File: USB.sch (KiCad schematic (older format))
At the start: 23 parts, among them J302 USB_B_Micro, Q301 SS8050-G, Q302 SS8050-G, Q303 SS8050-G, U301 CP2102N-A01-GQFN24

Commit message: libs added
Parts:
- D302: symbol ESP-Audio-rescue:SP0503BAHT-Power_Protection -> ESP32-Eurorack-Audio-rescue:SP0503BAHT-Power_Protection-ESP-Audio-rescue
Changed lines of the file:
@@
 EESchema Schematic File Version 4
+LIBS:ESP32-Eurorack-Audio-cache
 EELAYER 29 0
 EELAYER END
@@
 	3200 3250 3700 3250
 $Comp
-L ESP-Audio-rescue:SP0503BAHT-Power_Protection D302
+L ESP32-Eurorack-Audio-rescue:SP0503BAHT-Power_Protection-ESP-Audio-rescue D302
 U 1 1 5B67424B
 P 3550 4000

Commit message: current
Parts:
- L301: value 600 -> 0
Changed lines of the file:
@@
 Title "ESP32 Eurorack Audio Module"
 Date "2019-03-27"
-Rev "B2-public"
+Rev "C"
 Comp "(c) Robert Manzke 2019"
 Comment1 "https://creativecommons.org/licenses/by-nc-sa/4.0/"
@@
 P 2900 4300
 F 0 "L301" H 3037 4346 50  0000 L CNN
-F 1 "600" H 3037 4255 50  0000 L CNN
+F 1 "0" H 3037 4255 50  0000 L CNN
 F 2 "Capacitor_SMD:C_0805_2012Metric" V 2830 4300 50  0001 C CNN
 F 3 "~" H 2900 4300 50  0001 C CNN

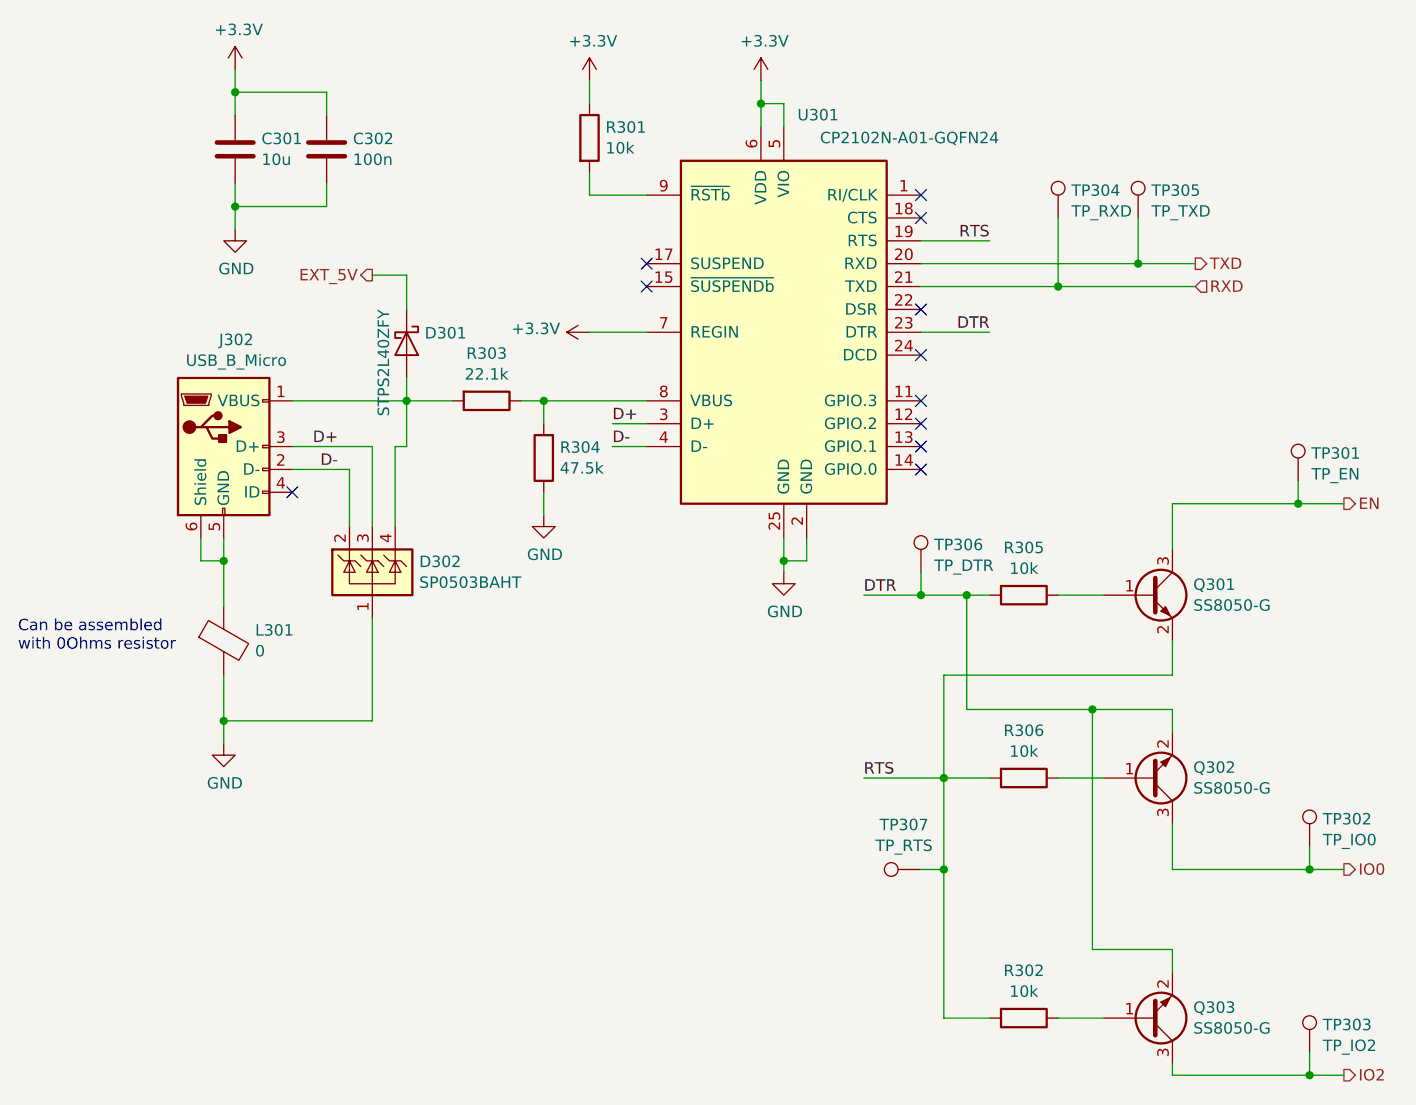
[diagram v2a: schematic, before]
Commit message: cleaned up schematic
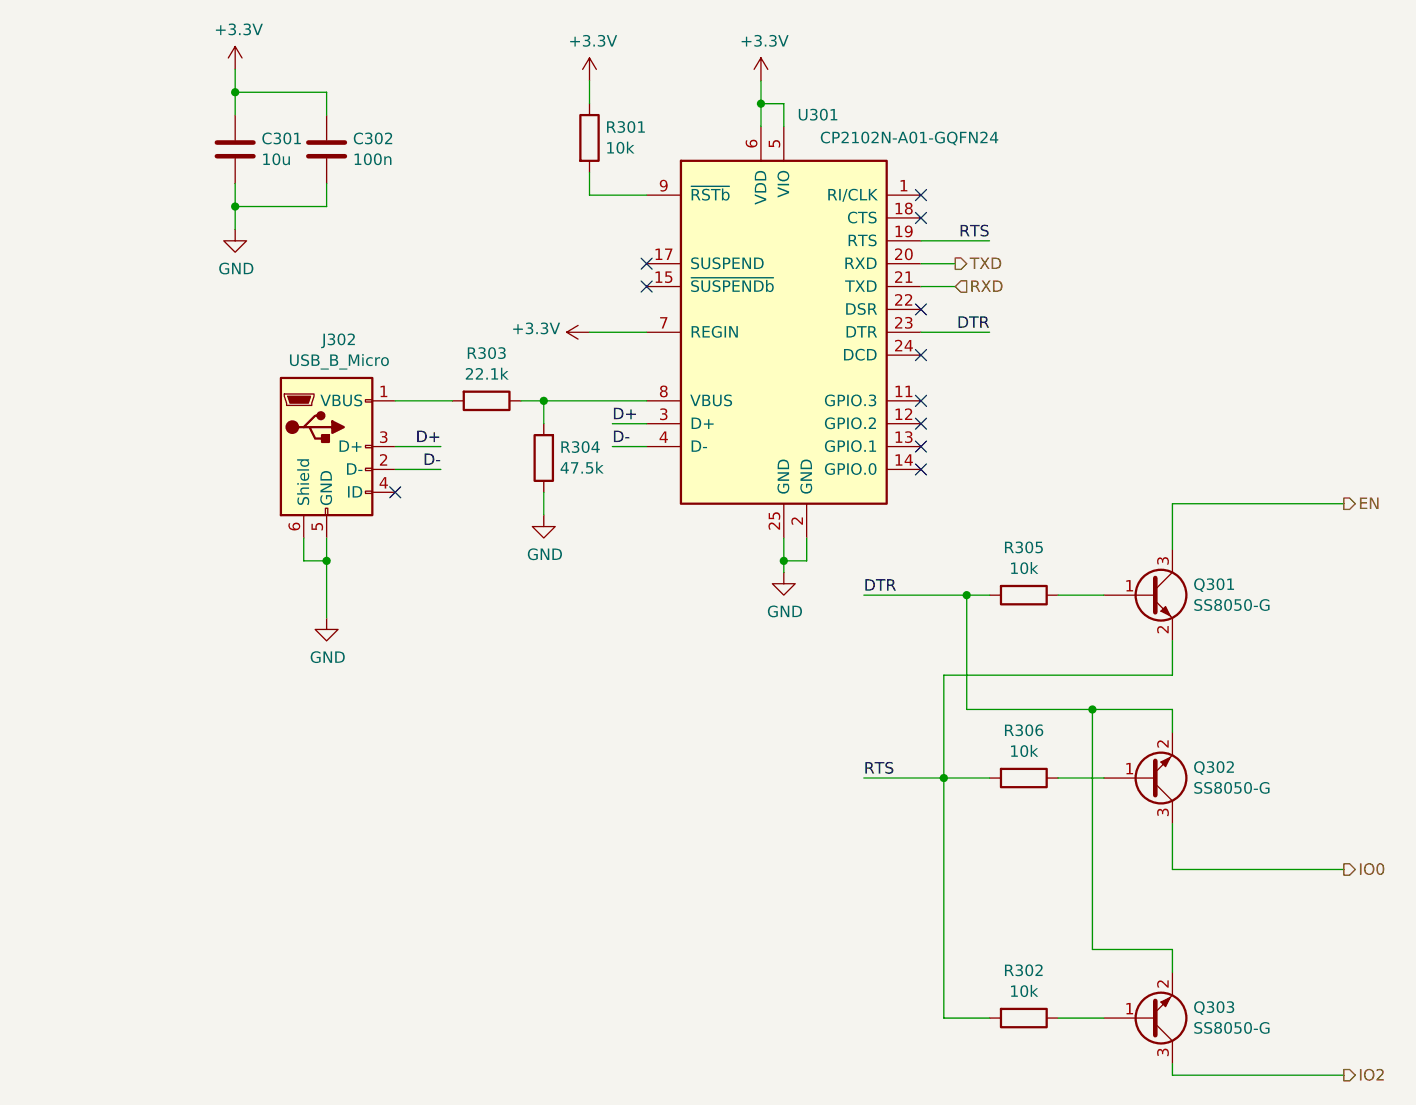
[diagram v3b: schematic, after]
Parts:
- removed D301: STPS2L40ZFY, Diode_SMD:D_SOD-123, symbol Device:D_Schottky
- removed D302: SP0503BAHT, Package_TO_SOT_SMD:SOT-143, symbol ESP32-Eurorack-Audio-rescue:SP0503BAHT-Power_Protection-ESP-Audio-rescue
- removed L301: 0, Capacitor_SMD:C_0805_2012Metric, symbol Device:Ferrite_Bead
- removed TP301: TP_EN, TestPoint:TestPoint_Keystone_5019_Minature, symbol Connector:TestPoint
- removed TP302: TP_IO0, TestPoint:TestPoint_Keystone_5019_Minature, symbol Connector:TestPoint
- removed TP303: TP_IO2, TestPoint:TestPoint_Keystone_5019_Minature, symbol Connector:TestPoint
- removed TP304: TP_RXD, TestPoint:TestPoint_Keystone_5019_Minature, symbol Connector:TestPoint
- removed TP305: TP_TXD, TestPoint:TestPoint_Keystone_5019_Minature, symbol Connector:TestPoint
- removed TP306: TP_DTR, TestPoint:TestPoint_Keystone_5019_Minature, symbol Connector:TestPoint
- removed TP307: TP_RTS, TestPoint:TestPoint_Keystone_5019_Minature, symbol Connector:TestPoint
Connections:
- net GND: now also J302.5 (GND), J302.6 (Shield)
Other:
- note removed: "Can be assembled \nwith 0Ohms resistor"
- moved on the sheet: J302
